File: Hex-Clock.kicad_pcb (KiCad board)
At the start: 2 copper layers, 77.1 x 89 mm, 18 parts

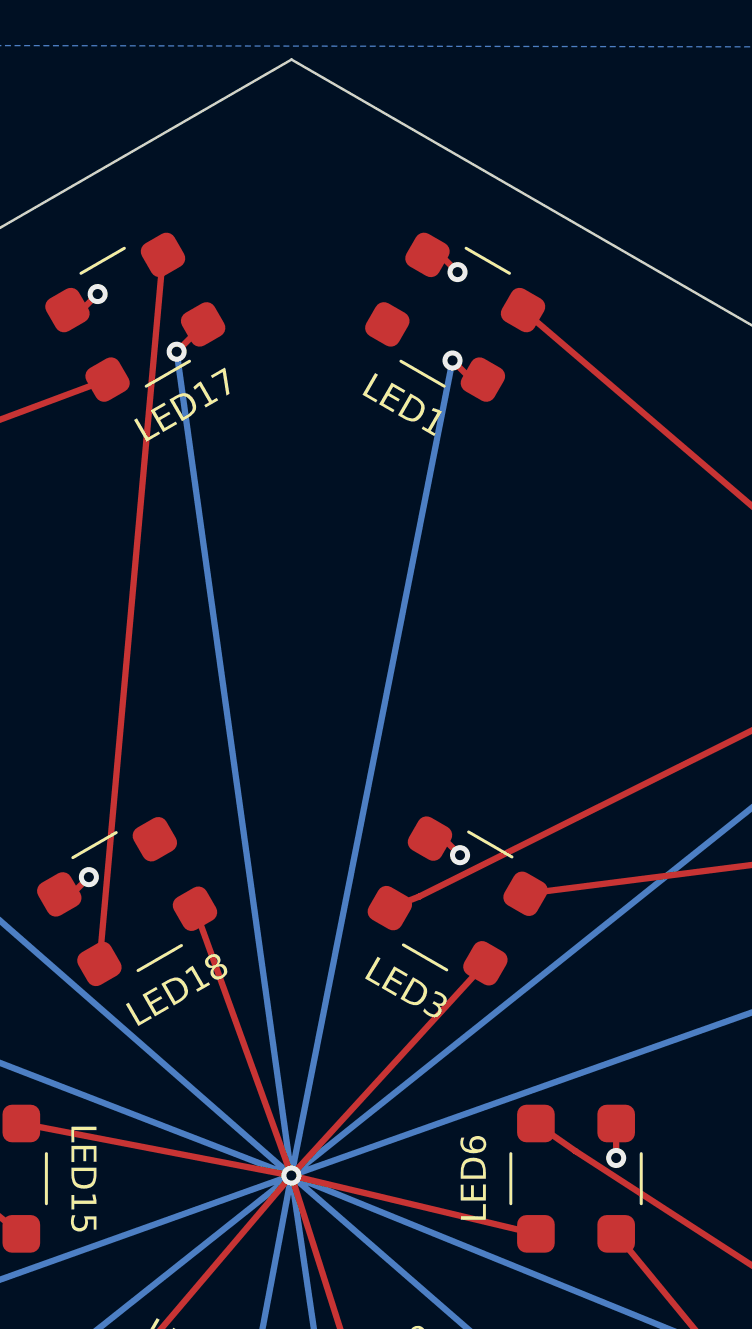
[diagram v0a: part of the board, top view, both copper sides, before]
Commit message: Added pads for DATA_IN and 5V
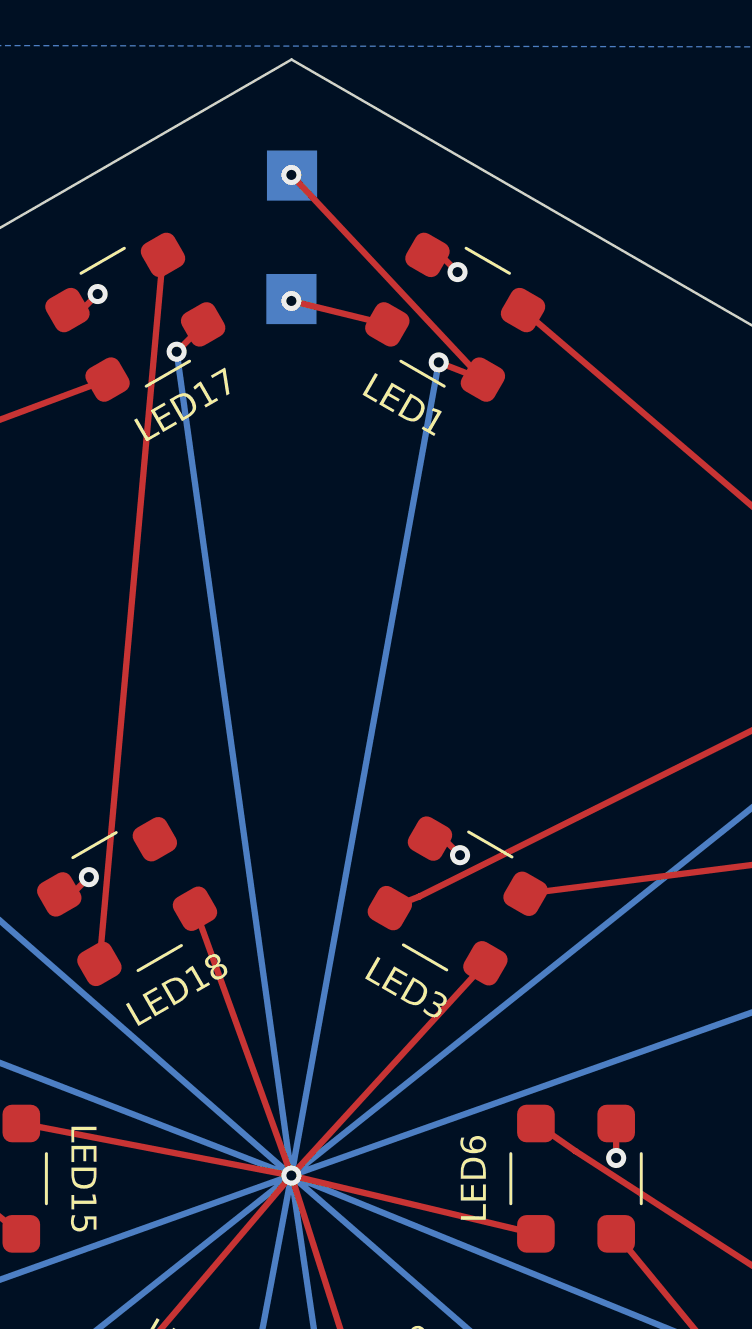
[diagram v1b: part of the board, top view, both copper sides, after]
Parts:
- added +5V: TestPoint_Pad_2.0x2.0mm, TestPoint:TestPoint_Pad_2.0x2.0mm, B.Cu at (150.2, 61.3)
- added DATA IN: TestPoint_Pad_2.0x2.0mm, TestPoint:TestPoint_Pad_2.0x2.0mm, B.Cu at (150.2, 66.2)
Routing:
- net +5V: track 480.4 -> 491.8 mm, vias 13 -> 14
- net Data IN: track 0.00 -> 3.94 mm, vias 0 -> 1
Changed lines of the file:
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@@
       (net 19 "Net-(LED14-Pad2)") (pinfunction "Data_IN") (pintype "input"))
+  )
+  (footprint "TestPoint:TestPoint_Pad_2.0x2.0mm" (layer "B.Cu")
+    (at 150.2 61.275 180)
+    (descr "SMD rectangular pad as test Point, square 2.0mm side length")
+    (tags "test point SMD pad rectangle square")
+    (attr exclude_from_pos_files exclude_from_bom)
+    (fp_text reference "+5V" (at 0 1.998) (layer "B.SilkS")
+      (effects (font (size 1 1) (thickness 0.15)) (justify mirror))
+    )
+    (fp_text value "TestPoint_Pad_2.0x2.0mm" (at 0 -2.05) (layer "B.Fab") hide
+      (effects (font (size 1 1) (thickness 0.15)) (justify mirror))
+    )
+    (fp_text user "${REFERENCE}" (at 0 2) (layer "B.Fab") hide
+      (effects (font (size 1 1) (thickness 0.15)) (justify mirror))
+    )
+    (fp_line (start 1.2 1.2) (end 1.2 -1.2) (layer "B.SilkS") (width 0.12))
+    (fp_line (start 1.2 -1.2) (end -1.2 -1.2) (layer "B.SilkS") (width 0.12))
+    (fp_line (start -1.2 -1.2) (end -1.2 1.2) (layer "B.SilkS") (width 0.12))
+    (fp_line (start -1.2 1.2) (end 1.2 1.2) (layer "B.SilkS") (width 0.12))
+    (fp_line (start -1.5 1.5) (end -1.5 -1.5) (layer "B.CrtYd") (width 0.05))
+    (fp_line (start 1.5 -1.5) (end 1.5 1.5) (layer "B.CrtYd") (width 0.05))
+    (fp_line (start 1.5 -1.5) (end -1.5 -1.5) (layer "B.CrtYd") (width 0.05))
+    (fp_line (start -1.5 1.5) (end 1.5 1.5) (layer "B.CrtYd") (width 0.05))
+    (pad "1" smd rect (at 0 0 180) (size 2 2) (layers "B.Cu" "B.Mask"))
+  )
+  (footprint "TestPoint:TestPoint_Pad_2.0x2.0mm" (layer "B.Cu")
+    (at 150.175 66.2 180)
+    (descr "SMD rectangular pad as test Point, square 2.0mm side length")
+    (tags "test point SMD pad rectangle square")
+    (attr exclude_from_pos_files exclude_from_bom)
+    (fp_text reference "DATA IN" (at 0 1.998) (layer "B.SilkS")
+      (effects (font (size 1 1) (thickness 0.15)) (justify mirror))
+    )
+    (fp_text value "TestPoint_Pad_2.0x2.0mm" (at 0 -2.05) (layer "B.Fab") hide
+      (effects (font (size 1 1) (thickness 0.15)) (justify mirror))
+    )
+    (fp_text user "${REFERENCE}" (at 0 2) (layer "B.Fab") hide
+      (effects (font (size 1 1) (thickness 0.15)) (justify mirror))
+    )
+    (fp_line (start 1.2 1.2) (end 1.2 -1.2) (layer "B.SilkS") (width 0.12))
+    (fp_line (start 1.2 -1.2) (end -1.2 -1.2) (layer "B.SilkS") (width 0.12))
+    (fp_line (start -1.2 -1.2) (end -1.2 1.2) (layer "B.SilkS") (width 0.12))
+    (fp_line (start -1.2 1.2) (end 1.2 1.2) (layer "B.SilkS") (width 0.12))
+    (fp_line (start -1.5 1.5) (end -1.5 -1.5) (layer "B.CrtYd") (width 0.05))
+    (fp_line (start 1.5 -1.5) (end 1.5 1.5) (layer "B.CrtYd") (width 0.05))
+    (fp_line (start 1.5 -1.5) (end -1.5 -1.5) (layer "B.CrtYd") (width 0.05))
+    (fp_line (start -1.5 1.5) (end 1.5 1.5) (layer "B.CrtYd") (width 0.05))
+    (pad "1" smd rect (at 0 0 180) (size 2 2) (layers "B.Cu" "B.Mask"))
   )
   (gr_line (start 188.719065 78.9) (end 150.180935 101.15) (layer "Dwgs.User") (width 0.1))
@@
   (segment (start 143.489359 132.614359) (end 144.125 133.25) (width 0.25) (layer "F.Cu") (net 1))
   (segment (start 181.425 114.064031) (end 181.425 115.15) (width 0.25) (layer "F.Cu") (net 1))
+  (segment (start 157.811191 69.410641) (end 156.05 68.725) (width 0.25) (layer "F.Cu") (net 1))
   (segment (start 146.655256 67.244744) (end 145.6 68.3) (width 0.25) (layer "F.Cu") (net 1))
   (segment (start 177.386191 80.960641) (end 176.210641 80.960641) (width 0.25) (layer "F.Cu") (net 1))
@@
   (segment (start 143.194744 109.364359) (end 143.310641 109.364359) (width 0.25) (layer "F.Cu") (net 1))
   (segment (start 126.605256 78.835641) (end 126.089359 78.835641) (width 0.25) (layer "F.Cu") (net 1))
-  (segment (start 157.811191 69.410641) (end 157.360641 69.410641) (width 0.25) (layer "F.Cu") (net 1))
   (segment (start 153.494744 111.564359) (end 150.175 101.15) (width 0.25) (layer "F.Cu") (net 1))
   (segment (start 143.194744 109.364359) (end 150.175 101.15) (width 0.25) (layer "F.Cu") (net 1))
   (segment (start 159.925 103.475) (end 150.175 101.15) (width 0.25) (layer "F.Cu") (net 1))
   (segment (start 146.655256 67.210641) (end 146.655256 67.244744) (width 0.25) (layer "F.Cu") (net 1))
+  (segment (start 157.811191 69.410641) (end 150.175 61.25) (width 0.25) (layer "F.Cu") (net 1))
   (segment (start 119.4 88.975) (end 119.85 89.425) (width 0.25) (layer "F.Cu") (net 1))
   (segment (start 139.405935 99.075) (end 150.175 101.15) (width 0.25) (layer "F.Cu") (net 1))
@@
   (segment (start 126.089359 78.835641) (end 125.425 79.5) (width 0.25) (layer "F.Cu") (net 1))
   (segment (start 157.911191 92.685641) (end 157.911191 93.138809) (width 0.25) (layer "F.Cu") (net 1))
-  (segment (start 157.360641 69.410641) (end 156.6 68.65) (width 0.25) (layer "F.Cu") (net 1))
   (segment (start 119.4 87.95) (end 119.4 88.975) (width 0.25) (layer "F.Cu") (net 1))
   (segment (start 142.919744 132.614359) (end 143.489359 132.614359) (width 0.25) (layer "F.Cu") (net 1))
@@
   (via (at 119.85 89.425) (size 0.8) (drill 0.4) (layers "F.Cu" "B.Cu") (free) (net 1))
   (via (at 181.45 90.075) (size 0.8) (drill 0.4) (layers "F.Cu" "B.Cu") (free) (net 1))
+  (via (at 150.175 61.25) (size 0.8) (drill 0.4) (layers "F.Cu" "B.Cu") (free) (net 1))
   (via (at 144.125 133.25) (size 0.8) (drill 0.4) (layers "F.Cu" "B.Cu") (free) (net 1))
   (via (at 150.175 101.15) (size 0.8) (drill 0.4) (layers "F.Cu" "B.Cu") (free) (net 1))
   (via (at 125.425 79.5) (size 0.8) (drill 0.4) (layers "F.Cu" "B.Cu") (free) (net 1))
-  (via (at 156.6 68.65) (size 0.8) (drill 0.4) (layers "F.Cu" "B.Cu") (free) (net 1))
+  (via (at 156.05 68.725) (size 0.8) (drill 0.4) (layers "F.Cu" "B.Cu") (free) (net 1))
   (via (at 145.6 68.3) (size 0.8) (drill 0.4) (layers "F.Cu" "B.Cu") (free) (net 1))
   (via (at 175.275 122.975) (size 0.8) (drill 0.4) (layers "F.Cu" "B.Cu") (free) (net 1))
@@
   (segment (start 124.002495 121.929097) (end 150.175 101.15) (width 0.25) (layer "B.Cu") (net 1))
   (segment (start 175.875 80.625) (end 150.175 101.15) (width 0.25) (layer "B.Cu") (net 1))
+  (segment (start 156.05 68.725) (end 150.175 101.15) (width 0.25) (layer "B.Cu") (net 1))
   (segment (start 181.075702 113.714733) (end 150.175 101.15) (width 0.25) (layer "B.Cu") (net 1))
-  (segment (start 156.6 68.65) (end 150.175 101.15) (width 0.25) (layer "B.Cu") (net 1))
   (segment (start 175.275 122.975) (end 150.175 101.15) (width 0.25) (layer "B.Cu") (net 1))
   (segment (start 144.125 133.25) (end 150.175 101.15) (width 0.25) (layer "B.Cu") (net 1))
@@
   (via (at 116.2 90.975) (size 0.8) (drill 0.4) (layers "F.Cu" "B.Cu") (free) (net 3))
   (via (at 142.1 89.25) (size 0.8) (drill 0.4) (layers "F.Cu" "B.Cu") (free) (net 3))
+  (segment (start 154.000679 67.210641) (end 150.175 66.275) (width 0.25) (layer "F.Cu") (net 4))
+  (via (at 150.175 66.275) (size 0.8) (drill 0.4) (layers "F.Cu" "B.Cu") (free) (net 4))
   (segment (start 155.275 90.025) (end 154.100679 90.485641) (width 0.25) (layer "F.Cu") (net 5))
   (segment (start 178.986191 78.189359) (end 155.275 90.025) (width 0.25) (layer "F.Cu") (net 5))
@@
     (connect_pads (clearance 0.508))
     (min_thickness 0.254) (filled_areas_thickness no)
-    (fill (thermal_gap 0.508) (thermal_bridge_width 0.508))
+    (fill yes (thermal_gap 0.508) (thermal_bridge_width 0.508))
     (polygon
       (pts
